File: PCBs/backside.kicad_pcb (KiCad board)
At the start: 2 copper layers, 45 parts, among them J1 9Pin, J3 Power, J5 Matrix, J7 Driver output 2, J9 Driver output 1, U1 HT1632C-52LQFP, U2 HT1632C-52LQFP, U3 STM32F103C8T6

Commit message: Finished routing, updated comm channel displays
Decided to use (and again modify) open hornet's com channel indicators. Finished routing traces and adding ground planes on the main board, though it may be a little sloppy. Began work on the back side board, which will have the LED drivers and STM32. Re added the shift register board for now for the sake of having more pins.
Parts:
- added A1: ShiftRegisterBoard, UFC:ShiftRegisterBoardPins, F.Cu at (39.4, 135.9)
- added C10: .1uF, Capacitor_SMD:C_0603_1608Metric_Pad1.08x0.95mm_HandSolder, F.Cu at (78.5, 181.6)
- added C3: .1uF, Capacitor_SMD:C_0603_1608Metric_Pad1.08x0.95mm_HandSolder, F.Cu at (69.8, 179.1)
- added C4: .1uF, Capacitor_SMD:C_0603_1608Metric_Pad1.08x0.95mm_HandSolder, F.Cu at (69.8, 181.6)
- added C5: .1uF, Capacitor_SMD:C_0603_1608Metric_Pad1.08x0.95mm_HandSolder, F.Cu at (74.2, 179.1)
- added C6: .1uF, Capacitor_SMD:C_0603_1608Metric_Pad1.08x0.95mm_HandSolder, F.Cu at (69.8, 184.1)
- added C7: .1uF, Capacitor_SMD:C_0603_1608Metric_Pad1.08x0.95mm_HandSolder, F.Cu at (74.2, 181.6)
- added C8: .1uF, Capacitor_SMD:C_0603_1608Metric_Pad1.08x0.95mm_HandSolder, F.Cu at (78.5, 179.1)
- added C9: .1uF, Capacitor_SMD:C_0603_1608Metric_Pad1.08x0.95mm_HandSolder, F.Cu at (74.2, 184.1)
- added J10: Conn_01x08_Male, Connector_PinSocket_2.54mm:PinSocket_1x08_P2.54mm_Vertical, F.Cu at (139.0, 128.3)
- added J11: Conn_01x09_Male, Connector_PinSocket_2.54mm:PinSocket_1x09_P2.54mm_Vertical, F.Cu at (131.4, 128.3)
- added J12: Conn_01x08_Male, Connector_PinSocket_2.54mm:PinSocket_1x08_P2.54mm_Vertical, F.Cu at (-24.8, 128.3)
- added J13: Conn_01x09_Male, Connector_PinSocket_2.54mm:PinSocket_1x09_P2.54mm_Vertical, F.Cu at (-32.4, 128.3)
- added J14: Conn_01x07_Male, Connector_PinSocket_2.54mm:PinSocket_1x07_P2.54mm_Vertical, F.Cu at (86.9, 152.3)
- added J15: Conn_01x07_Male, Connector_PinSocket_2.54mm:PinSocket_1x07_P2.54mm_Vertical, F.Cu at (91.0, 152.1)
- added J16: Conn_01x07_Male, Connector_PinSocket_2.54mm:PinSocket_1x07_P2.54mm_Vertical, F.Cu at (95.6, 152.1)
- added J17: Conn_01x04_Male, Connector_PinSocket_2.54mm:PinSocket_1x04_P2.54mm_Vertical, F.Cu at (104.8, 152.1)
- added J4: Conn_01x17_Male, Connector_PinSocket_2.54mm:PinSocket_1x17_P2.54mm_Vertical, F.Cu at (19.0, 152.4)
- added J6: Conn_01x17_Male, Connector_PinSocket_2.54mm:PinSocket_1x17_P2.54mm_Vertical, F.Cu at (19.0, 156.1)
- added J8: Conn_01x04_Male, Connector_PinSocket_2.54mm:PinSocket_1x04_P2.54mm_Vertical, F.Cu at (100.2, 152.1)
- added MH1: MountingHole_3.2mm_M3, MountingHole:MountingHole_3.2mm_M3, F.Cu at (125.1, 52.1)
- added MH2: MountingHole_3.2mm_M3, MountingHole:MountingHole_3.2mm_M3, F.Cu at (121.3, 148.6)
- added MH3: MountingHole_3.2mm_M3, MountingHole:MountingHole_3.2mm_M3, F.Cu at (-13.4, 148.6)
- added MH4: MountingHole_3.2mm_M3, MountingHole:MountingHole_3.2mm_M3, F.Cu at (-10.8, 52.1)
- J9: value Driver output 1 -> Conn_01x30_Male; footprint Connector_PinSocket_2.54mm:PinSocket_1x33_P2.54mm_Vertical -> Connector_PinSocket_2.54mm:PinSocket_1x30_P2.54mm_Vertical
- moved U2 163.4 mm to (3.17, 93.3), turned to 180 degrees
- moved U1 160.7 mm to (51.4, 88.3), turned to 90 degrees
- moved R32 160.4 mm to (5.08, 117.0), turned to 270 degrees
- moved C2 158.2 mm to (-9.12, 98.4), turned to 180 degrees
- moved R31 150.3 mm to (8.89, 113.2), turned to 270 degrees
- moved R27 145.6 mm to (24.1, 99.1)
- moved R28 145.5 mm to (18.6, 99.1)
- moved R22 141.9 mm to (25.6, 85.1)
- moved R30 141.6 mm to (11.4, 109.4), turned to 270 degrees
- moved R21 138.9 mm to (23.5, 90.2)
- moved R26 138.8 mm to (19.2, 102.9)
- moved R20 138.6 mm to (18.4, 92.1)
- moved R1 134.6 mm to (59.1, 115.6), turned to 270 degrees
- moved R34 133.7 mm to (1.91, 108.8), turned to 270 degrees
- moved R25 133.5 mm to (18.0, 95.9)
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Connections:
- J7 pad 10: /COM9-2 -> /M2
- J7 pad 11: /COM10-2 -> /F2
- J7 pad 12: /COM11-2 -> /K2
- J7 pad 13: /COM12-2 -> /COM4-2
- J7 pad 14: /COM13-2 -> /COM5-2
- J7 pad 15: /COM14-2 -> /COM6-2
- J7 pad 16: /COM15-2 -> /COM7-2
- J7 pad 17: /DOT2 -> /J2
- J7 pad 18: /DP2 -> /Q2
- J7 pad 19: /Q2 -> /G2
- J7 pad 20: /P2 -> /E2
- J7 pad 21: /N2 -> /COM8-2
- J7 pad 22: /M2 -> /COM9-2
- J7 pad 23: /L2 -> /COM10-2
- J7 pad 24: /K2 -> /COM11-2
- J7 pad 25: /J2 -> /L2
- J7 pad 26: /H2 -> /D2
- J7 pad 27: /G2 -> /C2
- J7 pad 28: /F2 -> /B2
- J7 pad 29: /E2 -> /A2
- J7 pad 30: /D2 -> /COM12-2
- J7 pad 31: /C2 -> /COM13-2
- J7 pad 32: /B2 -> /COM14-2
- J7 pad 33: /A2 -> /COM15-2
- J7 pad 5: /COM4-2 -> /DOT2
- J7 pad 6: /COM5-2 -> /DP2
- J7 pad 7: /COM6-2 -> /H2
- J7 pad 8: /COM7-2 -> /P2
- J7 pad 9: /COM8-2 -> /N2
- J9 pad 1: /A1 -> /COM12-1
- J9 pad 10: /K1 -> /M1
- J9 pad 12: /M1 -> /K1
- J9 pad 13: /N1 -> /J1
- J9 pad 14: /P1 -> /H1
- J9 pad 15: /Q1 -> /E1
- J9 pad 16: /DP1 -> /F1
- J9 pad 17: /DOT1 -> /G1
- J9 pad 18: /COM15-1 -> /D1
- J9 pad 19: /COM14-1 -> /C1
- J9 pad 2: /B1 -> /COM11-1
- J9 pad 20: /COM13-1 -> /B1
- J9 pad 21: /COM12-1 -> /A1
- J9 pad 22: /COM11-1 -> /COM8-1
- J9 pad 23: /COM10-1 -> /COM7-1
- J9 pad 24: /COM9-1 -> /COM6-1
- J9 pad 25: /COM8-1 -> /COM5-1
- J9 pad 26: /COM7-1 -> /COM4-1
- J9 pad 27: /COM6-1 -> /COM3-1
- J9 pad 28: /COM5-1 -> /COM2-1
- J9 pad 29: /COM4-1 -> /COM1-1
- J9 pad 3: /C1 -> /COM10-1
- J9 pad 30: /COM3-1 -> /COM0-1
- J9 pad 4: /D1 -> /COM9-1
- J9 pad 5: /E1 -> /DOT1
- J9 pad 6: /F1 -> /DP1
- J9 pad 7: /G1 -> /Q1
- J9 pad 8: /H1 -> /P1
- J9 pad 9: /J1 -> /N1
- U3 pad 10: Net-(U3-Pad10) -> Net-(R35-Pad2)
- U3 pad 11: Net-(R35-Pad2) -> /Analog1
- U3 pad 12: Net-(U3-Pad12) -> /Analog2
- U3 pad 13: /ROW4 -> /Analog3
- U3 pad 14: /ROW3 -> /Analog4
- U3 pad 15: /ROW2 -> /Analog5
- U3 pad 16: /ROW1 -> /Analog6
- U3 pad 17: /ROW0 -> /Analog7
- U3 pad 25: Net-(U3-Pad25) -> /CS1
- U3 pad 26: Net-(U3-Pad26) -> /CS2
- U3 pad 27: Net-(U3-Pad27) -> /WR
- U3 pad 28: Net-(U3-Pad28) -> /RD
- U3 pad 29: Net-(U3-Pad29) -> /DATA
- U3 pad 30: Net-(U3-Pad30) -> /DigInt4
- U3 pad 31: Net-(U3-Pad31) -> /DigInt3
- U3 pad 32: Net-(U3-Pad32) -> /DigInt2
- U3 pad 33: Net-(U3-Pad33) -> /DigInt1
- U3 pad 38: Net-(U3-Pad38) -> /SRCS
- U3 pad 39: /SW24 -> /SRCLK
- U3 pad 40: /SW23 -> /SRMISO
- U3 pad 41: /SW22 -> /ROW4
- U3 pad 42: /SW21 -> /ROW3
- U3 pad 43: /SW20 -> /ROW2
- U3 pad 45: /SW19 -> /ROW1
- U3 pad 46: /SW18 -> /ROW0

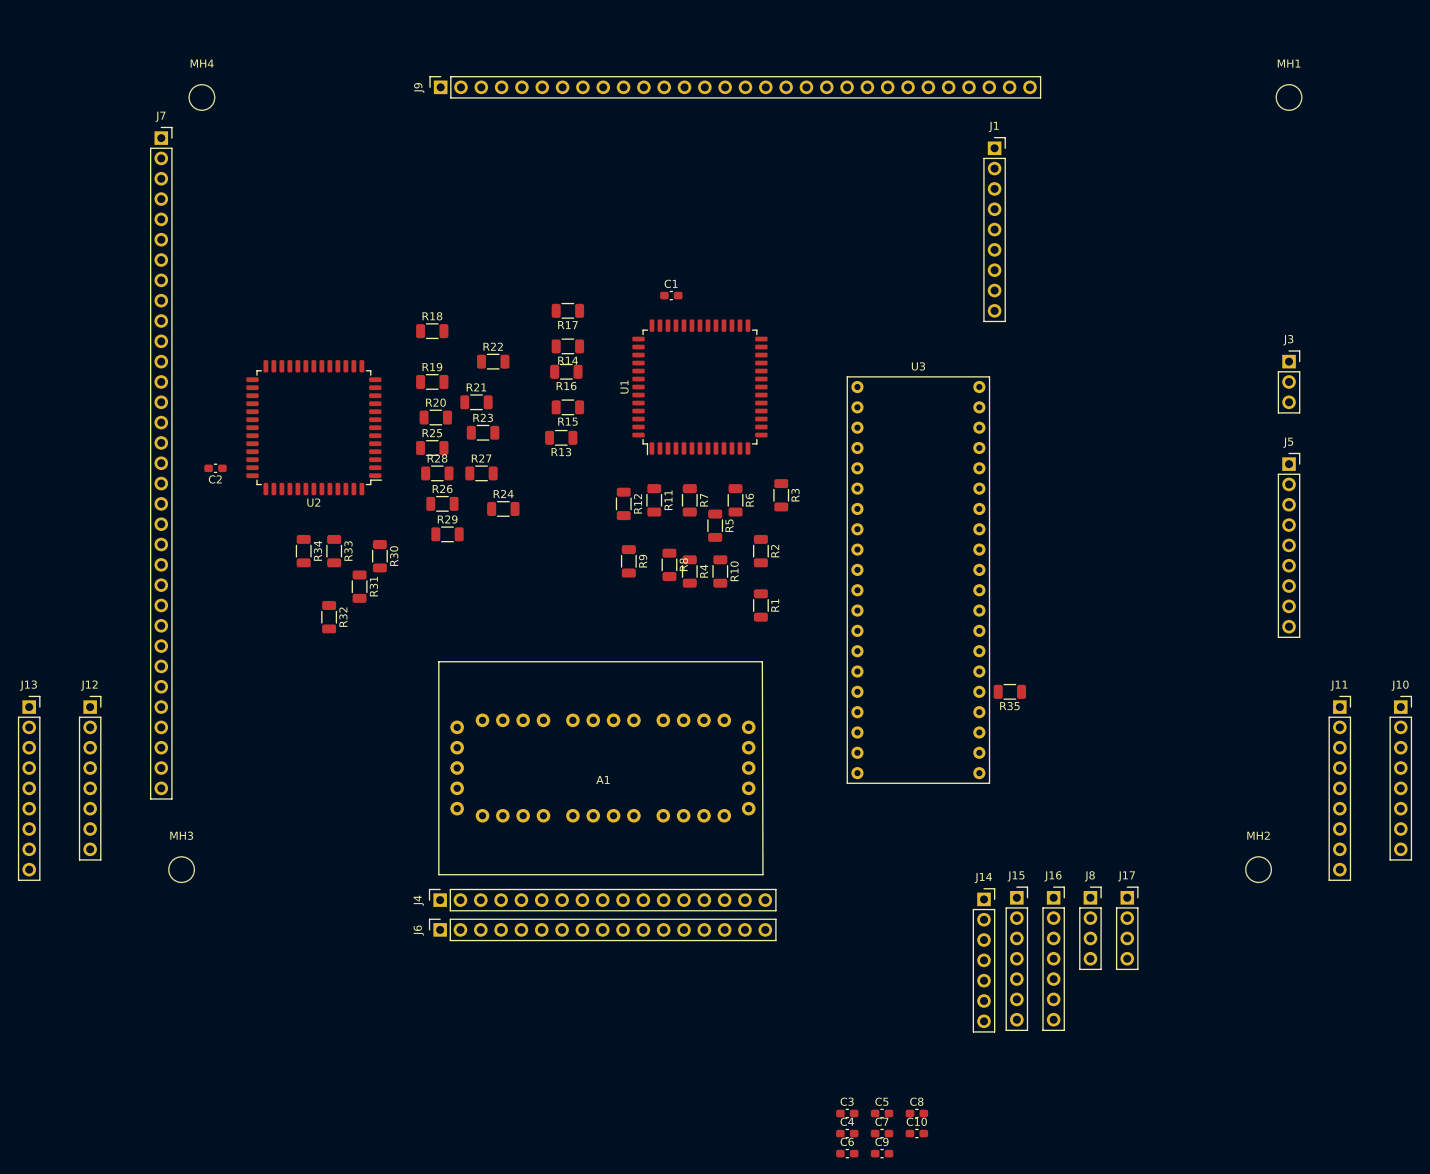
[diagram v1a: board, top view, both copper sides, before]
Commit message: Routed back side board
Routed the LED drivers, pin headers, shift registers, etc. that are on the back side. ECAD is close to done, and I will start on the MCAD at this point.
-Decided to avoid routing anodes and common cathodes to each of the comm channel displays, as that would probably have required at least an extra layer, instead I added a header to plug crimped wires directly into the front side.
-Some of the headers are two single width pin headers put side by side, meaning their courtyards overlap. I may redo this to use one footprint for both in the future.
-Still undecided on a couple part values
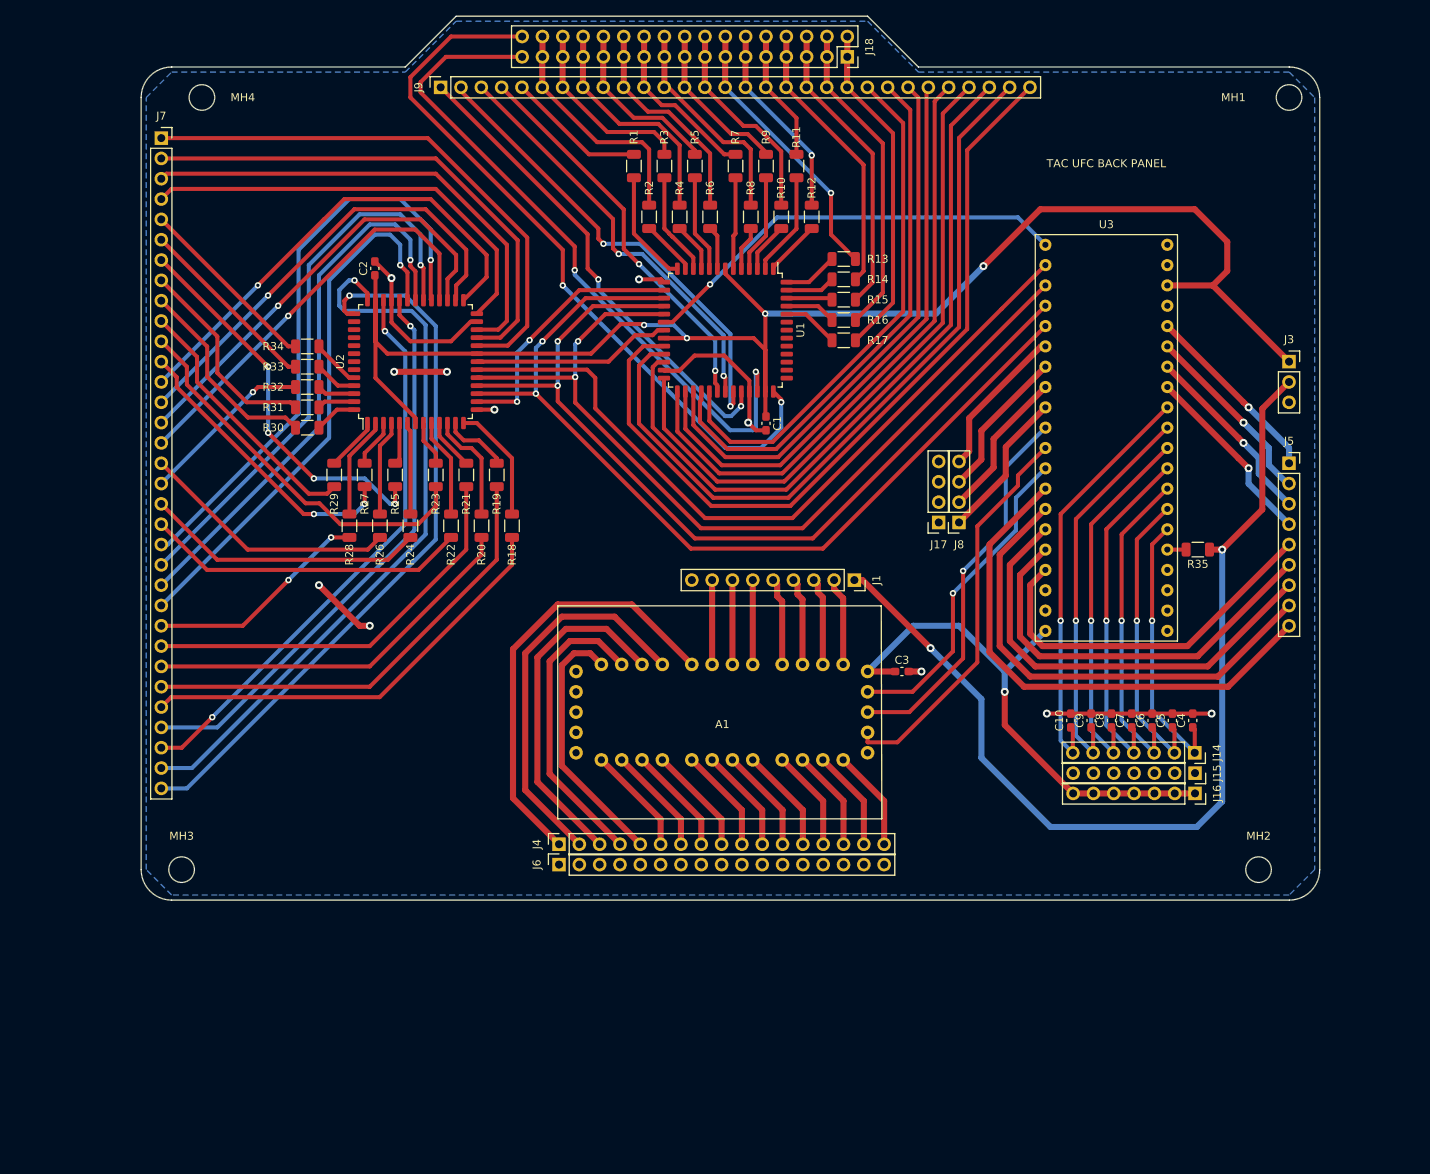
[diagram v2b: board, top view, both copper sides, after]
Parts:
- removed J10, J12: Conn_01x08_Male, Connector_PinSocket_2.54mm:PinSocket_1x08_P2.54mm_Vertical
- removed J11, J13: Conn_01x09_Male, Connector_PinSocket_2.54mm:PinSocket_1x09_P2.54mm_Vertical
- added J18: Conn_02x17_Odd_Even, Connector_PinSocket_2.54mm:PinSocket_2x17_P2.54mm_Vertical, F.Cu at (69.8, 47.0)
- moved C4 67.3 mm to (113.0, 129.9), turned to 90 degrees
- moved C6 66.2 mm to (108.0, 129.9), turned to 90 degrees
- moved C5 61.1 mm to (110.5, 129.9), turned to 90 degrees
- moved C7 60.3 mm to (105.4, 129.9), turned to 90 degrees
- moved C9 60.1 mm to (100.3, 129.9), turned to 90 degrees
- moved R1 57.2 mm to (43.2, 60.6), turned to 90 degrees
- moved J1 56.7 mm to (70.7, 112.4), turned to 270 degrees
- moved C3 55.7 mm to (76.7, 123.8)
- moved C10 55.1 mm to (97.8, 129.9), turned to 90 degrees
- moved C8 54.8 mm to (102.9, 129.9), turned to 90 degrees
- moved J17 52.5 mm to (81.3, 105.2), turned to 180 degrees
- moved R9 52.3 mm to (59.7, 60.6), turned to 90 degrees
- moved J8 49.7 mm to (83.8, 105.2), turned to 180 degrees
- moved R11 45.4 mm to (63.5, 60.6), turned to 90 degrees
- moved R5 45.0 mm to (50.8, 60.6), turned to 90 degrees
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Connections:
- J4 pad 1: /DIN1 -> /DIN17
- J4 pad 10: /DIN10 -> /DIN5
- J4 pad 11: /DIN11 -> /DIN6
- J4 pad 12: /DIN12 -> /DIN7
- J4 pad 13: /DIN13 -> /DIN8
- J4 pad 14: /DIN14 -> /DIN9
- J4 pad 15: /DIN15 -> /DIN10
- J4 pad 16: /DIN16 -> /DIN11
- J4 pad 17: /DIN17 -> /DIN12
- J4 pad 2: /DIN2 -> /DIN16
- J4 pad 3: /DIN3 -> /DIN15
- J4 pad 4: /DIN4 -> /DIN14
- J4 pad 5: /DIN5 -> /DIN13
- J4 pad 6: /DIN6 -> /DIN1
- J4 pad 7: /DIN7 -> /DIN2
- J4 pad 8: /DIN8 -> /DIN3
- J4 pad 9: /DIN9 -> /DIN4
- R1 pad 2: /A1 -> /DOT1
- R10 pad 2: /K1 -> /H1
- R11 pad 2: /L1 -> /G1
- R12 pad 2: /M1 -> /F1
- R13 pad 2: /N1 -> /E1
- R14 pad 2: /P1 -> /D1
- R15 pad 2: /Q1 -> /C1
- R16 pad 2: /DP1 -> /B1
- R17 pad 2: /DOT1 -> /A1
- R2 pad 2: /B1 -> /DP1
- R3 pad 2: /C1 -> /Q1
- R4 pad 2: /D1 -> /P1
- R5 pad 2: /E1 -> /N1
- R6 pad 2: /F1 -> /M1
- R7 pad 2: /G1 -> /L1
- R8 pad 2: /H1 -> /K1
- U3 pad 27: /WR -> /RD
- U3 pad 28: /RD -> /WR
- U3 pad 52: Net-(U3-Pad52) -> /3.3V
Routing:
- net /3.3V: track 0.00 -> 263.4 mm, vias 0 -> 5
- net /LEDPWM: track 0.00 -> 121.9 mm, vias 0 -> 2
- net /DATA: track 0.00 -> 115.1 mm, vias 0 -> 2
- net /WR: track 0.00 -> 112.8 mm, vias 0 -> 2
- net /RD: track 0.00 -> 110.5 mm, vias 0 -> 2
- net /COM0-1: track 0.00 -> 102.2 mm
- net /COM1-1: track 0.00 -> 96.2 mm
- net /CS2: track 0.00 -> 94.1 mm
- net /COM14-1: track 0.00 -> 91.7 mm, vias 0 -> 2
- net /COM14-2: track 0.00 -> 90.6 mm, vias 0 -> 1
- net /COM2-1: track 0.00 -> 89.9 mm
- net /COM15-2: track 0.00 -> 89.8 mm, vias 0 -> 1
- net /COM13-1: track 0.00 -> 86.4 mm, vias 0 -> 2
- net /GND: track 0.00 -> 84.6 mm, vias 0 -> 11
- net /COM3-1: track 0.00 -> 82.9 mm
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- added copper zone on B.Cu, net /GND
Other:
- board outline added: 147.3 x 110.5 mm
- board text added: "TAC UFC BACK PANEL"
